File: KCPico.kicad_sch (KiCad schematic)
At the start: 17 parts, among them J1 Conn_01x04_Pin, J2 Conn_01x04_Pin, J3 Conn_01x05_Pin, J4 AudioJack3, J5 Conn_01x04_Pin, SW1 SW_Omron_B3FS, SW2 SW_Omron_B3FS, U1 CH559L

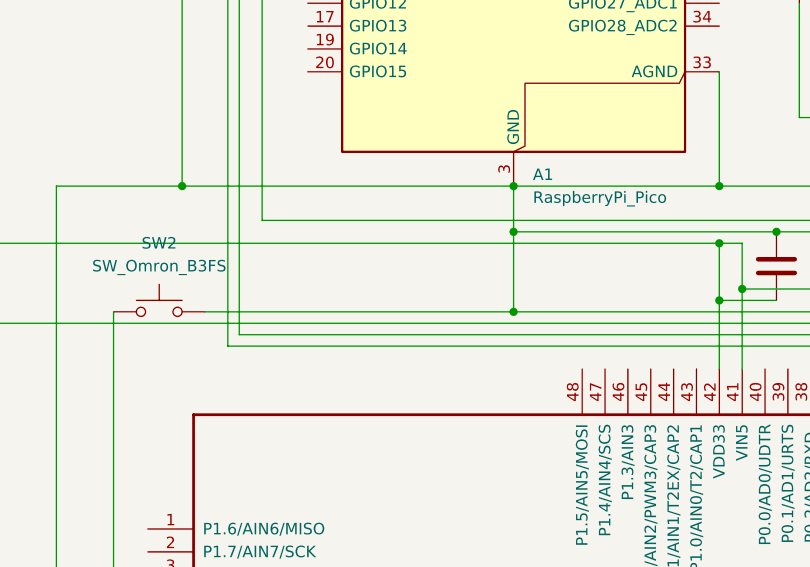
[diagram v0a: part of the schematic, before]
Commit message: Hardware: add SW3 Omron B3FS tactile switch on RP2040 AIN3
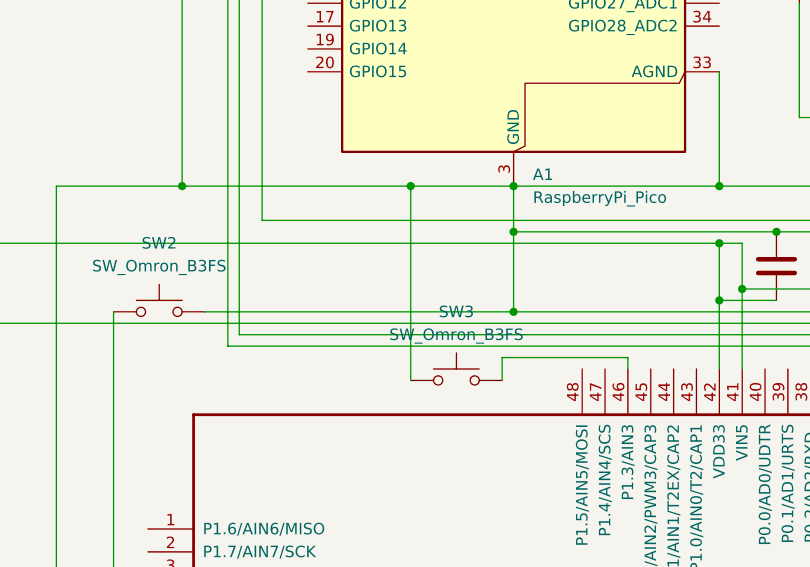
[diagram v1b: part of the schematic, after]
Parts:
- added SW3: SW_Omron_B3FS, Button_Switch_THT:SW_TH_Tactile_Omron_B3F-100x, symbol Switch:SW_Omron_B3FS
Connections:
- net at A1.13 (GND), A1.18 (GND), A1.23 (GND)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: now also SW3.1
- net at U1.46 (P1.3/AIN3): now also SW3.2
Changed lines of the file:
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@@
+	)
+	(junction
+		(at 69.85 107.95)
+		(diameter 0)
+		(color 0 0 0 0)
 	)
 	(junction
@@
 	(wire
 		(pts
+			(xy 69.85 107.95) (xy 81.28 107.95)
+		)
+		(stroke
+			(width 0)
+			(type default)
+		)
+	)
+	(wire
+		(pts
 			(xy 45.72 29.21) (xy 45.72 64.77)
 		)
@@
 	(wire
 		(pts
+			(xy 93.98 127) (xy 80.01 127)
+		)
+		(stroke
+			(width 0)
+			(type default)
+		)
+	)
+	(wire
+		(pts
 			(xy 172.72 170.18) (xy 165.1 170.18)
 		)
@@
 	(wire
 		(pts
+			(xy 69.85 129.54) (xy 69.85 107.95)
+		)
+		(stroke
+			(width 0)
+			(type default)
+		)
+	)
+	(wire
+		(pts
+			(xy 80.01 127) (xy 80.01 129.54)
+		)
+		(stroke
+			(width 0)
+			(type default)
+		)
+	)
+	(wire
+		(pts
 			(xy 137.16 127) (xy 175.26 127)
 		)
@@
 	(wire
 		(pts
-			(xy 44.45 107.95) (xy 81.28 107.95)
+			(xy 44.45 107.95) (xy 69.85 107.95)
 		)
 		(stroke
@@
 		(pts
 			(xy 132.08 55.88) (xy 132.08 107.95)
+		)
+		(stroke
+			(width 0)
+			(type default)
+		)
+	)
+	(wire
+		(pts
+			(xy 93.98 128.27) (xy 93.98 127)
 		)
 		(stroke
@@
 					(unit 1)
 				)
+			)
+		)
+	)
+	(symbol
+		(lib_id "Switch:SW_Omron_B3FS")
+		(at 74.93 129.54 0)
+		(unit 1)
+		(body_style 1)
+		(exclude_from_sim no)
+		(in_bom yes)
+		(on_board yes)
+		(in_pos_files yes)
+		(dnp no)
+		(fields_autoplaced yes)
+		(property "Reference" "SW3"
+			(at 74.93 121.92 0)
+			(show_name no)
+			(do_not_autoplace no)
+			(effects
+				(font
+					(size 1.27 1.27)
+				)
+			)
+		)
+		(property "Value" "SW_Omron_B3FS"
+			(at 74.93 124.46 0)
+			(show_name no)
+			(do_not_autoplace no)
+			(effects
+				(font
+					(size 1.27 1.27)
+				)
+			)
+		)
+		(property "Footprint" "Button_Switch_THT:SW_TH_Tactile_Omron_B3F-100x"
+			(at 74.93 124.46 0)
+			(hide yes)
+			(show_name no)
+			(do_not_autoplace no)
+			(effects
+				(font
+					(size 1.27 1.27)
+				)
+			)
+		)
+		(property "Datasheet" "https://omronfs.omron.com/en_US/ecb/products/pdf/en-b3fs.pdf"
+			(at 74.93 124.46 0)
+			(hide yes)
+			(show_name no)
+			(do_not_autoplace no)
+			(effects
+				(font
+					(size 1.27 1.27)
+				)
+			)
+		)
+		(property "Description" "Omron B3FS 6x6mm single pole normally-open tactile switch"
+			(at 74.93 129.54 0)
+			(hide yes)
+			(show_name no)
+			(do_not_autoplace no)
+			(effects
+				(font
+					(size 1.27 1.27)
+				)
+			)
+		)
+		(pin "1"
+		)
+		(pin "2"
+		)
+		(instances
+			(project "KCPico"
+				(path "/ea41da54-d267-4f6f-b358-bca6d6d0aa3e"
+					(reference "SW3")
+					(unit 1)
+				)
